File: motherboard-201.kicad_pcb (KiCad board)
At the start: 2 copper layers, 216 x 150 mm, 106 parts, among them J1 PWR_conn, J2 PS2_CONN, J3 MSX_Slot, J4 MSX_Slot, J5 GFX_Connector_Output, J6 CONN_JOY, J7 CONN_JOY, J8 DIN8, K1 Relay, Q2 2N2907, U1 AS6C1008, U10 74HC670, U11 74HC670, U12 74HC670, U13 ATMEGA328P, U15 74HC139, U16 74LS07, U17 74HC74, U19 LM311, U2 TL7705, U20 SST39SF0, U23 74HC157, U24 AY-3-8910, U25 74HC157, U26 74HC138, U27 74HC153, U28 82C55A, U3 GAL_declogic-201, U4 74HC670, U5 74HC670, U6 Z84C00, U7 74HC74, U8 74HCT245, U9 74HC670, Y1 16Mhz

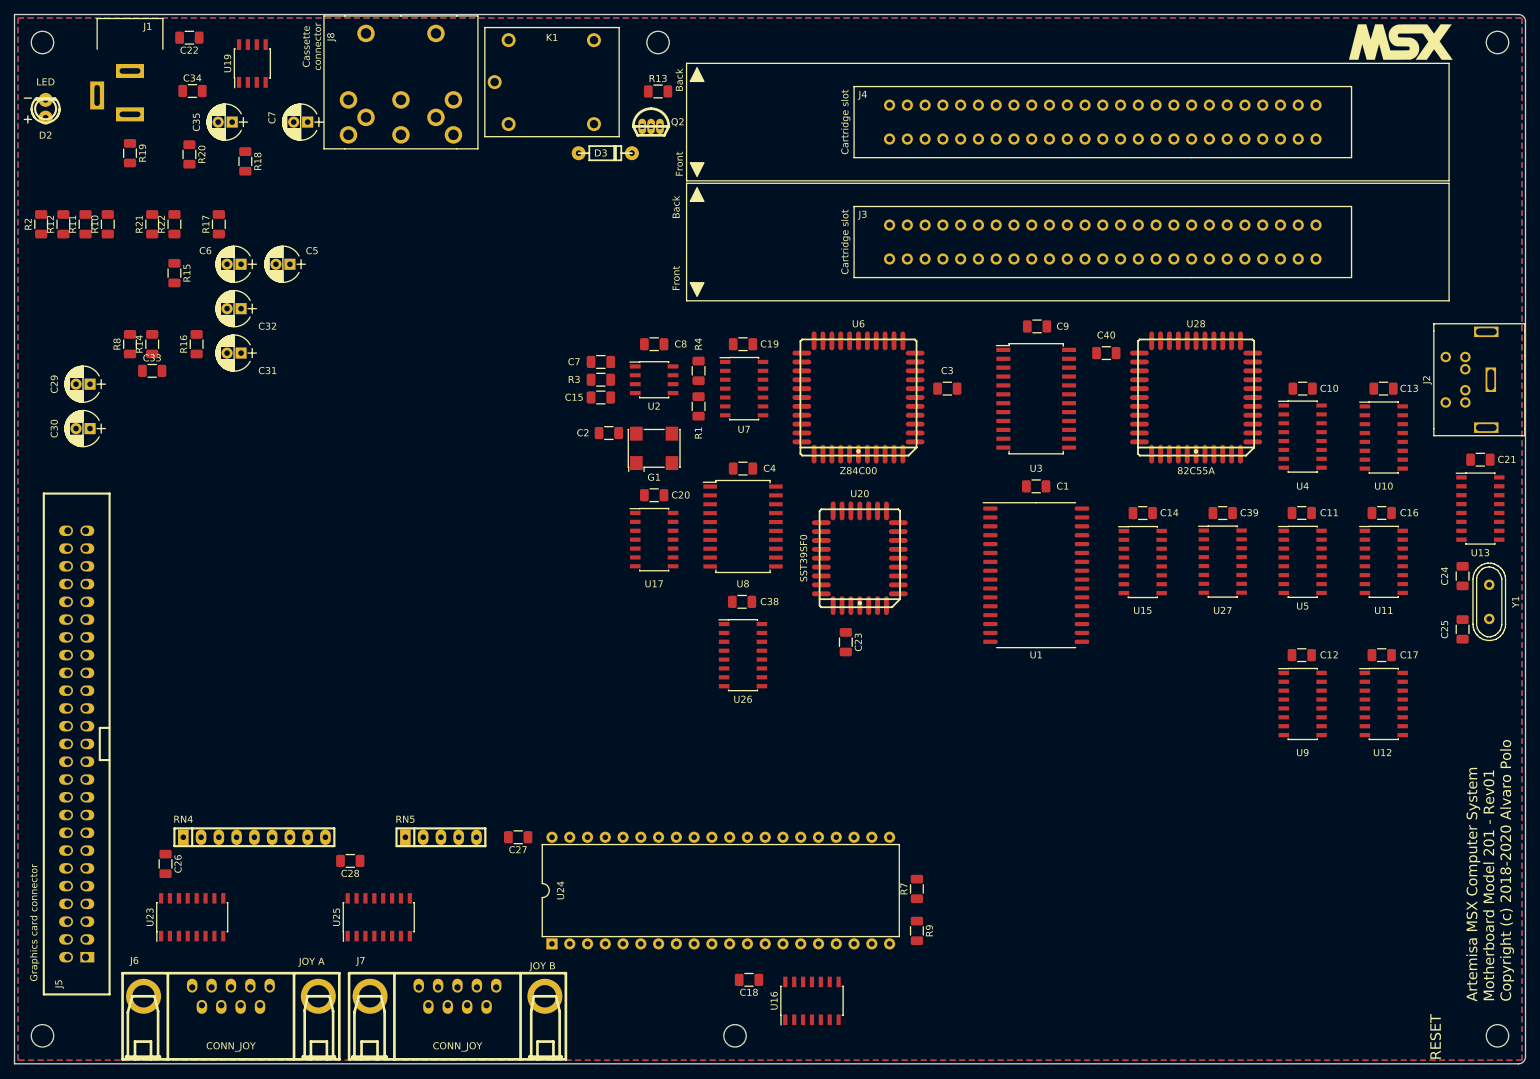
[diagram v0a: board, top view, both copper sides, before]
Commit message: Update to KiCad 6
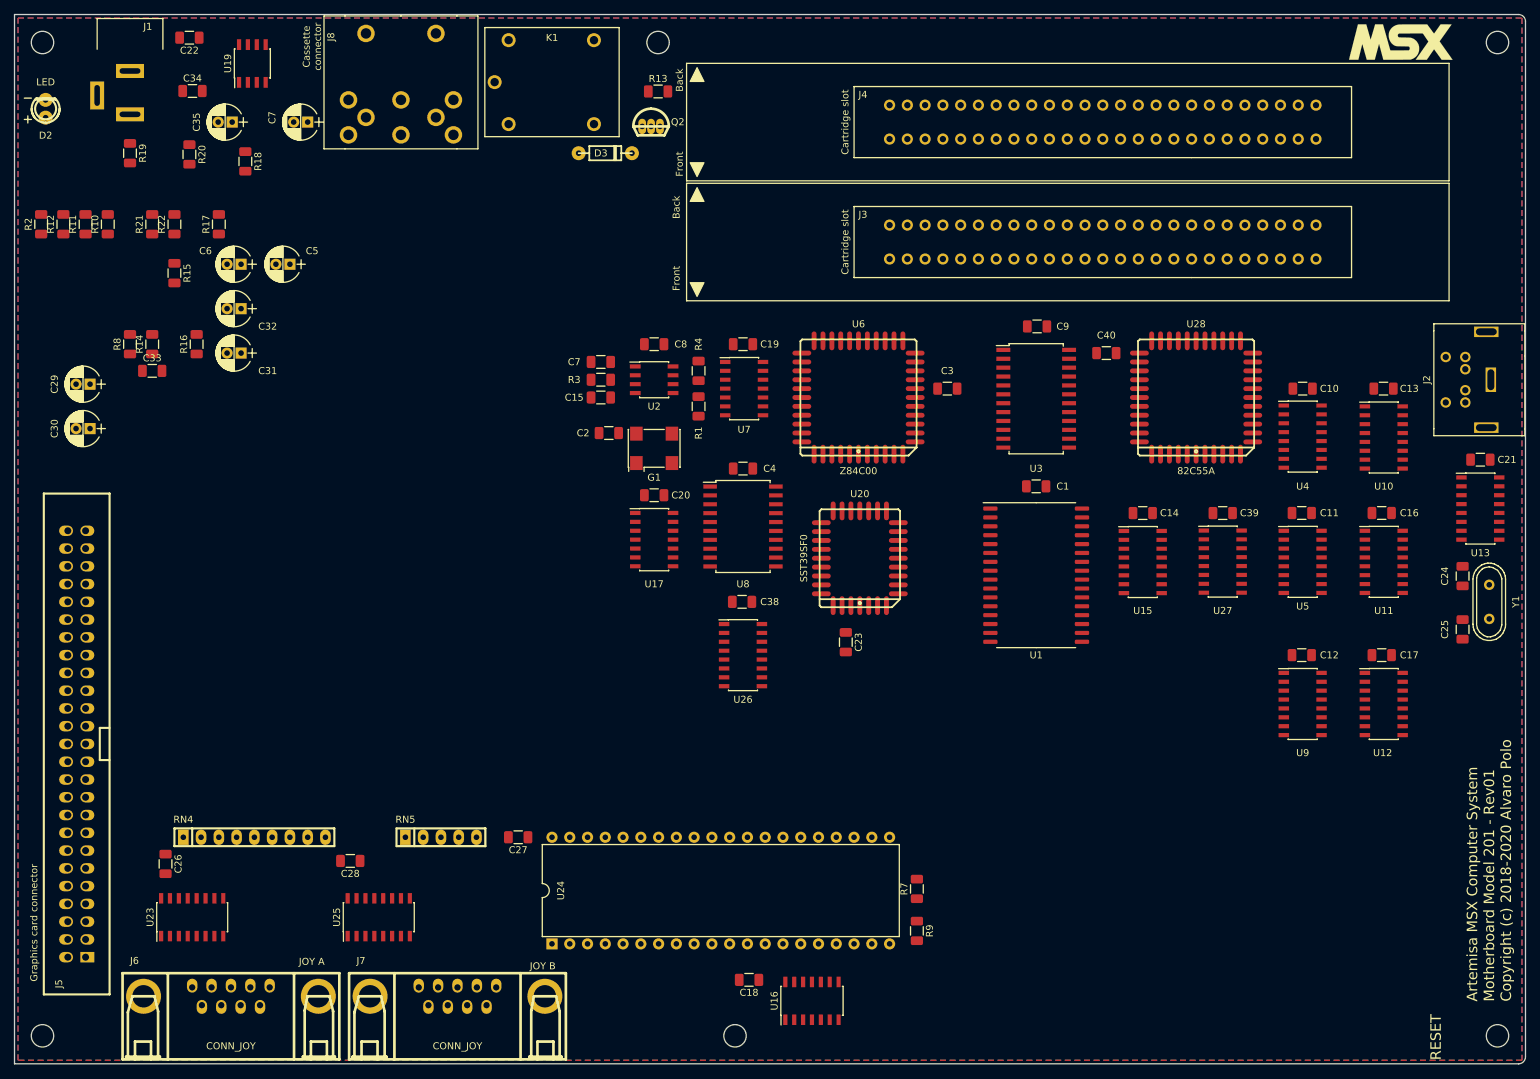
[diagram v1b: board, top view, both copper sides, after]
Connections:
- net /DECODING/~IOSL renamed /DECODING/~{IOSL}
- net /DECODING/~PPISL renamed /DECODING/~{PPISL}
- net /DECODING/~PSGSL renamed /DECODING/~{PSGSL}
- net /KBD/~RSL0 renamed /KBD/~{RSL0}
- net /KBD/~RSL1 renamed /KBD/~{RSL1}
- net /KBD/~RSL2 renamed /KBD/~{RSL2}
- net /KBD/~WSL0H renamed /KBD/~{WSL0H}
- net /KBD/~WSL0L renamed /KBD/~{WSL0L}
- net /KBD/~WSL1H renamed /KBD/~{WSL1H}
- net /KBD/~WSL1L renamed /KBD/~{WSL1L}
- net /KBD/~WSL2H renamed /KBD/~{WSL2H}
- net /KBD/~WSL2L renamed /KBD/~{WSL2L}
- net /~CAPSLOCK renamed /~{CAPSLOCK}
- net /~CASMOTOR renamed /~{CASMOTOR}
- net /~CS1 renamed /~{CS1}
- net /~CS12 renamed /~{CS12}
- net /~CS2 renamed /~{CS2}
- net /~INT renamed /~{INT}
- net /~IORQ renamed /~{IORQ}
- net /~KANALOCK renamed /~{KANALOCK}
- net /~M1 renamed /~{M1}
- net /~MREQ renamed /~{MREQ}
- net /~PPIRD renamed /~{PPIRD}
- net /~PPIRDY renamed /~{PPIRDY}
- net /~PPIWR renamed /~{PPIWR}
- net /~RD renamed /~{RD}
- net /~RESET renamed /~{RESET}
- net /~RFSH renamed /~{RFSH}
- net /~SLTSL0 renamed /~{SLTSL0}
- net /~SLTSL1 renamed /~{SLTSL1}
- net /~SLTSL2 renamed /~{SLTSL2}
- net /~SLTSL3 renamed /~{SLTSL3}
- net /~SLTSLEN renamed /~{SLTSLEN}
- net /~VDPSL renamed /~{VDPSL}
- net /~WAIT renamed /~{WAIT}
- net /~WR renamed /~{WR}
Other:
- net class Default removed
- net class Power removed
